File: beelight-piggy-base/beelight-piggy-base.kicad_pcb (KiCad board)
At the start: 2 copper layers, 55 x 55 mm, 67 parts, among them J10 USB C power only, J11 ExtWSSolderPads, J3 BatSolderPads, J4 WS2812_ext, J7 DevSide, Q1 AO3400A, SW1 SW_Push, U2 BMA253, U3 TPS22917LDBV, U4 rysta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

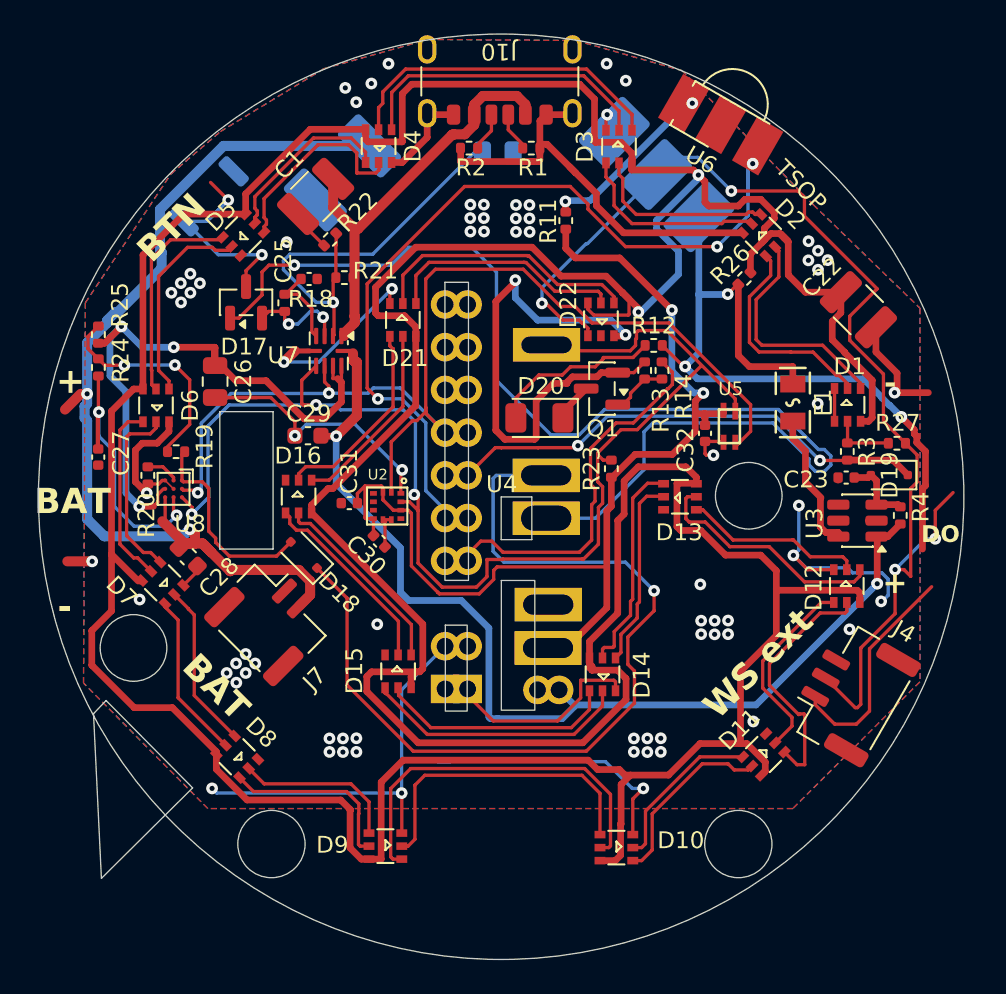
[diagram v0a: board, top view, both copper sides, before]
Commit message: PROTOTYPE ORDER - minor fixes + new board outline
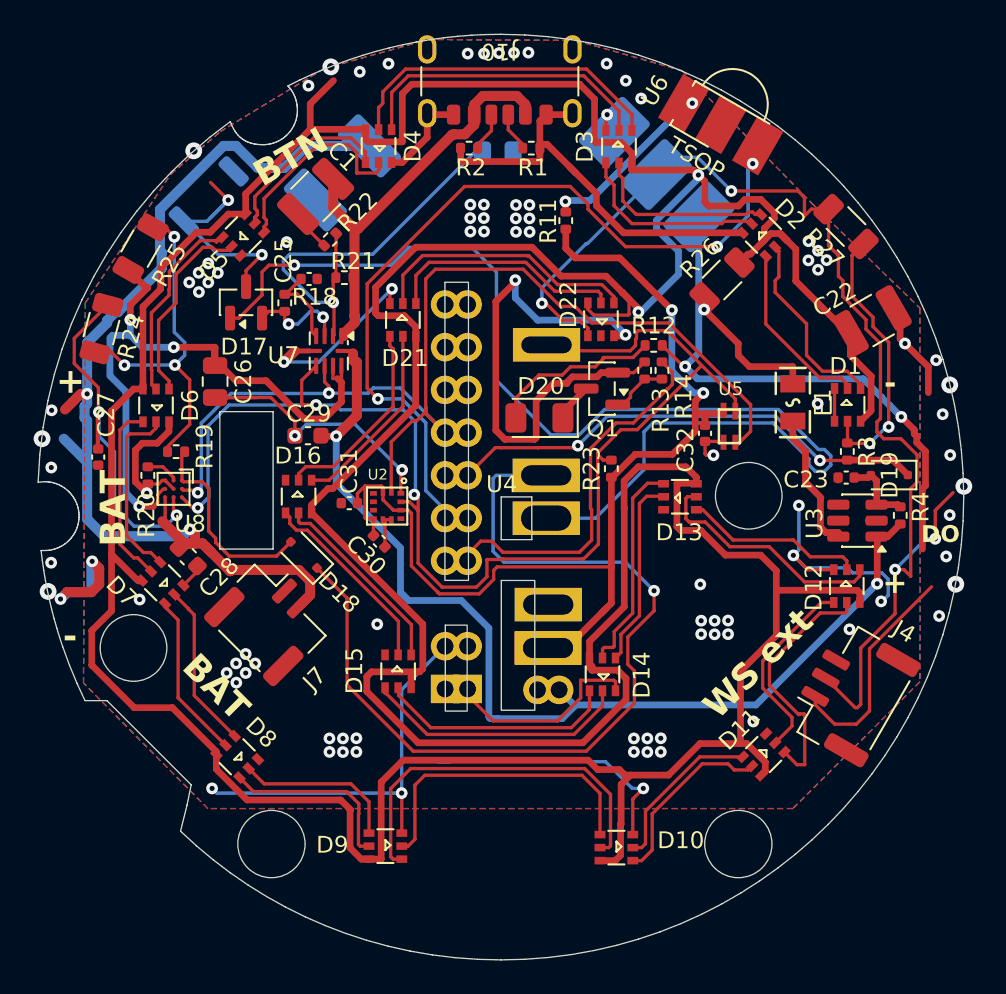
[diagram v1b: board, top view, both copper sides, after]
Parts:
- R24, R25, R26, R27: footprint Resistor_SMD:R_0402_1005Metric -> Resistor_SMD:R_1206_3216Metric
- moved R27 13.2 mm to (175.7, 79.3), turned to 135 degrees
- moved R25 5.70 mm to (133.8, 80.6), turned to 60 degrees
- moved R24 2.32 mm to (131.5, 85.3), turned to -105 degrees
- moved R26 1.33 mm to (168.4, 82.5)
- moved C22 1.04 mm to (177.3, 84.9), turned to 30 degrees
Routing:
- net Net-(D1-DI): track 3.69 -> 16.2 mm, vias 0 -> 2
- net Net-(R19-Pad1): track 13.1 -> 20.6 mm, vias 2 -> 3
- net Net-(U8-VDD): track 18.2 -> 23.9 mm
- net GND: track 187.0 -> 191.2 mm, vias 77 -> 86
- net BAT: track 62.5 -> 65.9 mm, vias 2 -> 5
- net Net-(U8-SRX): track 36.4 -> 39.3 mm
- net Net-(D1-BO): track 12.9 -> 10.6 mm
- net Net-(D1-DO): track 13.8 -> 11.6 mm
- net VLED: track 58.5 -> 56.5 mm, vias 3 -> 6
- net Net-(D5-DO): track 12.4 -> 11.4 mm
- net Net-(D22-DO): track 69.1 -> 69.9 mm, vias 4 -> 7
- net Net-(D1-VDD): track 297.4 -> 298.3 mm, vias 2 -> 5
- net SCL: track 74.9 -> 74.1 mm
- net +3.3V: track 61.8 -> 62.4 mm
- net Net-(D5-BO): track 12.2 -> 11.6 mm
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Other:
- outline, holes or cut-outs redrawn
